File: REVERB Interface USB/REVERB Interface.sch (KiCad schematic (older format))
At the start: 73 parts, among them J1 RPiZeroW, J2 Iridium, J3 APRS, J4 Antenna, J6 USB_B_Micro, J7 USB, J8 USBPOGO, M1 MountingHole_Pad, M2 MountingHole_Pad, M3 MountingHole_Pad, M4 MountingHole_Pad, M5 PiMount, M6 PiMount, M7 PiMount, M8 PiMount, U1 IMU, U2 MAX3232, U3 CY7C65213-28PVXI, U4 TXB0104D, U5 DS3232M

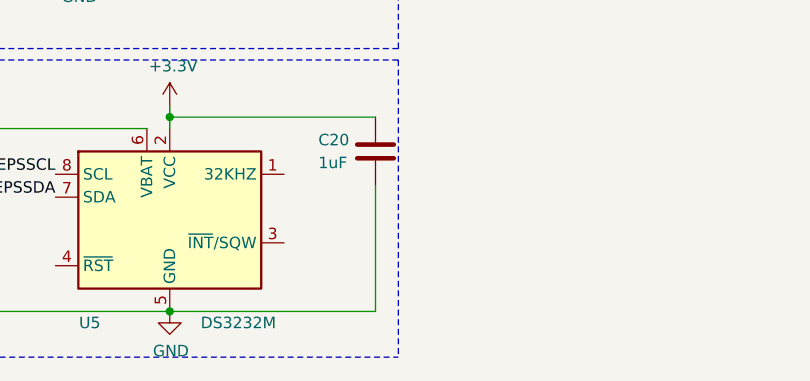
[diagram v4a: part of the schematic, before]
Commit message: add footprints, may need to use smaller battery
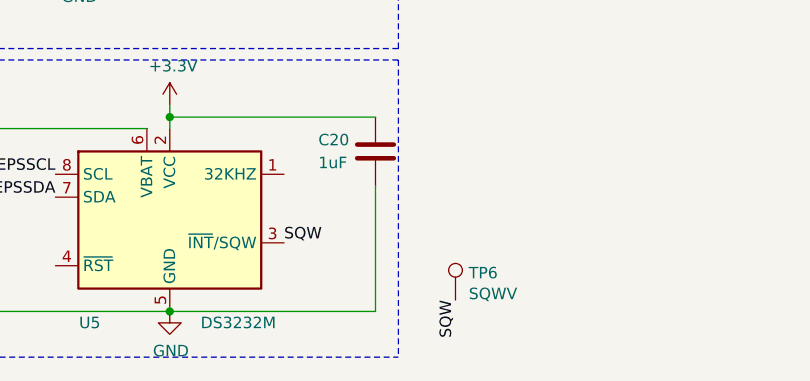
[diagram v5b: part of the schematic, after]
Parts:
- added TP6: SQWV, TestPoint:TestPoint_Pad_D2.0mm, symbol Connector:TestPoint
- BT1: footprint (none) -> REVERB Interface:CR2032-LINX-HLD-001-THM
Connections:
- net SQW: now reaches U5.3 (~INT~/SQW)
- net SQW: now also TP6.1
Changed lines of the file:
@@
 	6600 7000 4100 7000
 $Comp
-L Device:Battery_Cell BT1
-U 1 1 61948908
-P 4350 7700
-F 0 "BT1" H 4150 7850 50  0000 L CNN
-F 1 "CR-2032" H 4150 7650 50  0000 L CNN
-F 2 "" V 4350 7760 50  0001 C CNN
-F 3 "~" V 4350 7760 50  0001 C CNN
-	1    4350 7700
-	1    0    0    -1
-$EndComp
-$Comp
-L power:+3.3V #PWR?
+L power:+3.3V #PWR0135
 U 1 1 6194BC39
 P 5600 7200
-F 0 "#PWR?" H 5600 7050 50  0001 C CNN
+F 0 "#PWR0135" H 5600 7050 50  0001 C CNN
 F 1 "+3.3V" H 5615 7373 50  0000 C CNN
 F 2 "" H 5600 7200 50  0001 C CNN
@@
 	1    0    0    -1
 $EndComp
+Text Label 6100 7800 0    50   ~ 0
+SQW
+Text Label 6850 8050 3    50   ~ 0
+SQW
+$Comp
+L Connector:TestPoint TP6
+U 1 1 6194CAD9
+P 6850 8050
+F 0 "TP6" H 6908 8168 50  0000 L CNN
+F 1 "SQWV" H 6908 8077 50  0000 L CNN
+F 2 "TestPoint:TestPoint_Pad_D2.0mm" H 7050 8050 50  0001 C CNN
+F 3 "~" H 7050 8050 50  0001 C CNN
+	1    6850 8050
+	1    0    0    -1
+$EndComp
+$Comp
+L Device:Battery_Cell BT1
+U 1 1 61948908
+P 4350 7700
+F 0 "BT1" H 4150 7850 50  0000 L CNN
+F 1 "CR-2032" H 4150 7650 50  0000 L CNN
+F 2 "REVERB Interface:CR2032-LINX-HLD-001-THM" V 4350 7760 50  0001 C CNN
+F 3 "~" V 4350 7760 50  0001 C CNN
+	1    4350 7700
+	1    0    0    -1
+$EndComp

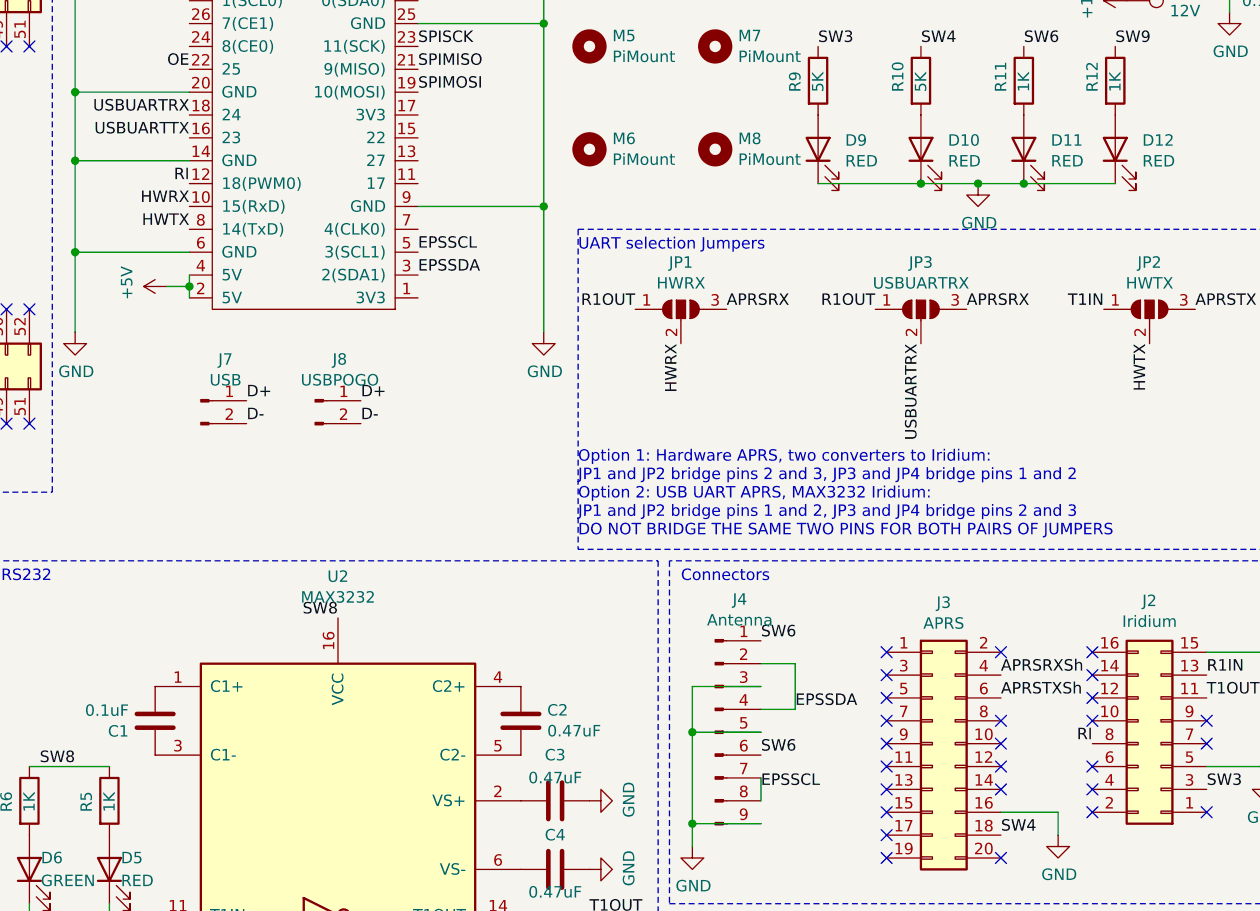
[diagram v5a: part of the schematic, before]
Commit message: Remove RI line
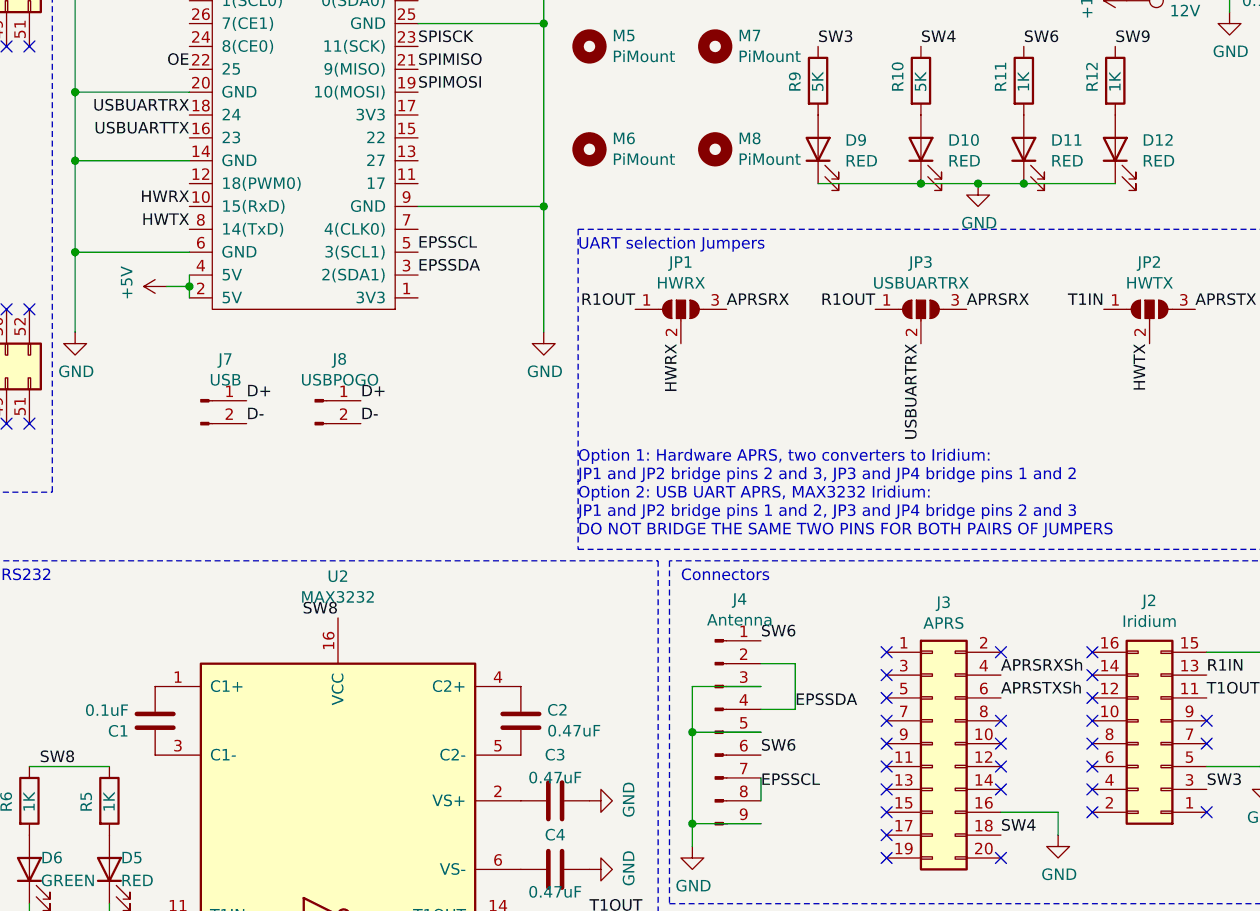
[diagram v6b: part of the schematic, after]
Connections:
- net RI: no longer names the net of J1.12 (18(PWM0))
- net RI: no longer J2.8 (Pin_8)
- no-connect marks 98 -> 99
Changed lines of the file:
@@
 Text Label 4550 1250 2    50   ~ 0
 IMURST
-Text Label 8500 4700 2    50   ~ 0
-RI
-Text Label 4550 2250 2    50   ~ 0
-RI
 Wire Wire Line
 	9250 4800 9250 4300
@@
 	1    0    0    -1
 $EndComp
+NoConn ~ 8500 4700
 $EndSCHEMATC

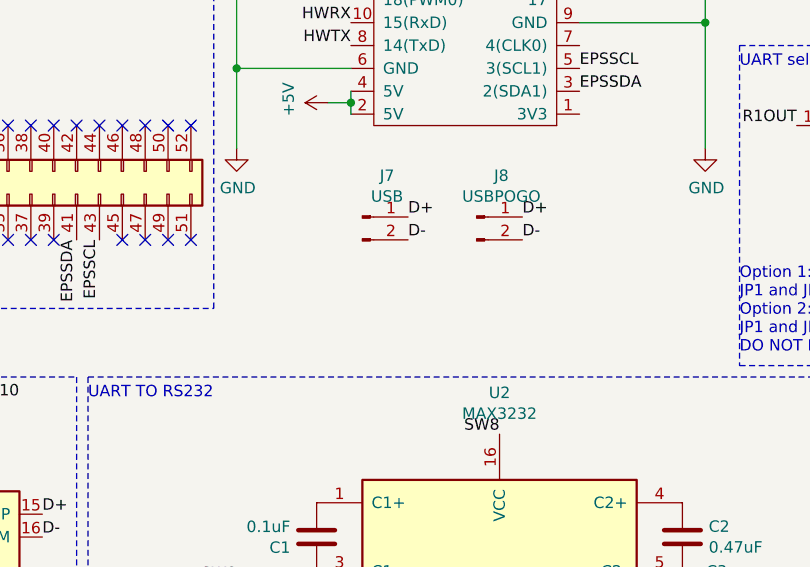
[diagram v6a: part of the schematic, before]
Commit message: add usb switch
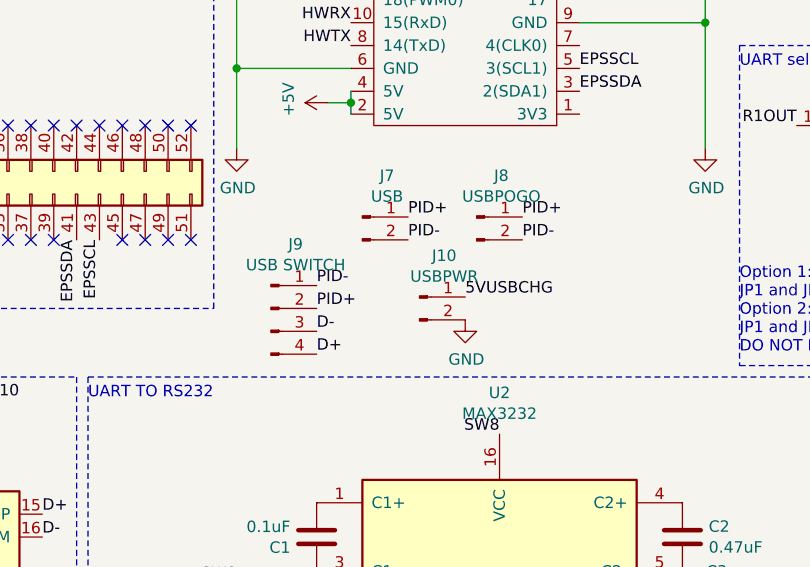
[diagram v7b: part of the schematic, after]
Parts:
- added J10: USBPWR, Connector_JST:JST_XH_B2B-XH-A_1x02_P2.50mm_Vertical, symbol Connector:Conn_01x02_Male
- added J9: USB SWITCH, Connector_JST:JST_XH_B4B-XH-A_1x04_P2.50mm_Vertical, symbol Connector:Conn_01x04_Male
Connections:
- net 5VUSBCHG: now also J10.1 (Pin_1)
- net D+: now also J9.4 (Pin_4); no longer J7.1 (Pin_1), J8.1 (Pin_1)
- net D-: now also J9.3 (Pin_3); no longer J7.2 (Pin_2), J8.2 (Pin_2)
- net GND: now also J10.2 (Pin_2)
- new net PID+: J7.1 (Pin_1), J8.1 (Pin_1), J9.2 (Pin_2)
- new net PID-: J7.2 (Pin_2), J8.2 (Pin_2), J9.1 (Pin_1)
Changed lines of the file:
@@
 $EndComp
 Text Label 4800 3200 0    50   ~ 0
-D+
+PID+
 Text Label 4800 3300 0    50   ~ 0
-D-
+PID-
 $Comp
 L Interface_UART:MAX3232 U2
@@
 $EndComp
 Text Label 5300 3200 0    50   ~ 0
-D+
+PID+
 Text Label 5300 3300 0    50   ~ 0
-D-
+PID-
 $Comp
 L Mechanical:MountingHole M5
@@
 $EndComp
 NoConn ~ 8500 4700
+$Comp
+L Connector:Conn_01x04_Male J9
+U 1 1 619777A4
+P 4200 3600
+F 0 "J9" H 4308 3881 50  0000 C CNN
+F 1 "USB SWITCH" H 4308 3790 50  0000 C CNN
+F 2 "Connector_JST:JST_XH_B4B-XH-A_1x04_P2.50mm_Vertical" H 4200 3600 50  0001 C CNN
+F 3 "~" H 4200 3600 50  0001 C CNN
+	1    4200 3600
+	1    0    0    -1
+$EndComp
+Text Label 4400 3600 0    50   ~ 0
+PID+
+Text Label 4400 3500 0    50   ~ 0
+PID-
+Text Label 4400 3800 0    50   ~ 0
+D+
+Text Label 4400 3700 0    50   ~ 0
+D-
+$Comp
+L Connector:Conn_01x02_Male J10
+U 1 1 61984053
+P 4850 3550
+F 0 "J10" H 4958 3731 50  0000 C CNN
+F 1 "USBPWR" H 4958 3640 50  0000 C CNN
+F 2 "Connector_JST:JST_XH_B2B-XH-A_1x02_P2.50mm_Vertical" H 4850 3550 50  0001 C CNN
+F 3 "~" H 4850 3550 50  0001 C CNN
+	1    4850 3550
+	1    0    0    -1
+$EndComp
+Text Label 5050 3550 0    50   ~ 0
+5VUSBCHG
+$Comp
+L power:GND #PWR0136
+U 1 1 6198E211
+P 5050 3650
+F 0 "#PWR0136" H 5050 3400 50  0001 C CNN
+F 1 "GND" H 5055 3477 50  0000 C CNN
+F 2 "" H 5050 3650 50  0001 C CNN
+F 3 "" H 5050 3650 50  0001 C CNN
+	1    5050 3650
+	1    0    0    -1
+$EndComp
 $EndSCHEMATC

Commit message: Move some parts around, remove UART LEDs, .step export, push v1.6
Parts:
- removed D1, D5: RED, LED_SMD:LED_0805_2012Metric_Pad1.15x1.40mm_HandSolder, symbol Device:LED
- removed D2, D6: GREEN, LED_SMD:LED_0805_2012Metric_Pad1.15x1.40mm_HandSolder, symbol Device:LED
- removed R1, R2, R5, R6: 1K, Resistor_SMD:R_0805_2012Metric_Pad1.20x1.40mm_HandSolder, symbol Device:R
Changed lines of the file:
@@
 Title "TJ REVERB Interface Board"
 Date "2021-10-03"
-Rev "1.5"
+Rev "1.6"
 Comp "TJ Nanosat Club"
 Comment1 "Redesign from previous Eagle designs"
@@
 $EndComp
 Wire Wire Line
-	2100 4700 1300 4700
-Wire Wire Line
-	2100 4800 1700 4800
-$Comp
-L Device:LED D1
-U 1 1 61680797
-P 1700 4450
-F 0 "D1" V 1739 4332 50  0000 R CNN
-F 1 "RED" V 1648 4332 50  0000 R CNN
-F 2 "LED_SMD:LED_0805_2012Metric_Pad1.15x1.40mm_HandSolder" H 1700 4450 50  0001 C CNN
-F 3 "~" H 1700 4450 50  0001 C CNN
-	1    1700 4450
-	0    -1   -1   0
-$EndComp
-$Comp
-L Device:LED D2
-U 1 1 61681979
-P 1300 4450
-F 0 "D2" V 1339 4332 50  0000 R CNN
-F 1 "GREEN" V 1248 4332 50  0000 R CNN
-F 2 "LED_SMD:LED_0805_2012Metric_Pad1.15x1.40mm_HandSolder" H 1300 4450 50  0001 C CNN
-F 3 "~" H 1300 4450 50  0001 C CNN
-	1    1300 4450
-	0    -1   -1   0
-$EndComp
-$Comp
-L Device:R R1
-U 1 1 61683EE4
-P 1700 4150
-F 0 "R1" V 1600 4100 50  0000 L CNN
-F 1 "1K" V 1700 4100 50  0000 L CNN
-F 2 "Resistor_SMD:R_0805_2012Metric_Pad1.20x1.40mm_HandSolder" V 1630 4150 50  0001 C CNN
-F 3 "~" H 1700 4150 50  0001 C CNN
-	1    1700 4150
-	1    0    0    -1
-$EndComp
-$Comp
-L Device:R R2
-U 1 1 6168462F
-P 1300 4150
-F 0 "R2" V 1200 4100 50  0000 L CNN
-F 1 "1K" V 1300 4100 50  0000 L CNN
-F 2 "Resistor_SMD:R_0805_2012Metric_Pad1.20x1.40mm_HandSolder" V 1230 4150 50  0001 C CNN
-F 3 "~" H 1300 4150 50  0001 C CNN
-	1    1300 4150
-	1    0    0    -1
-$EndComp
-Wire Wire Line
-	1300 4000 1700 4000
-Connection ~ 1700 4000
-Wire Wire Line
-	1700 4600 1700 4800
-Connection ~ 1700 4800
-Wire Wire Line
-	1700 4800 1200 4800
-Wire Wire Line
-	1300 4600 1300 4700
-Connection ~ 1300 4700
-Wire Wire Line
-	1300 4700 1200 4700
-Wire Wire Line
 	2600 4300 2600 4000
 $Comp
@@
 Wire Wire Line
 	3550 6100 4100 6100
-$Comp
-L Device:LED D5
-U 1 1 616CB109
-P 4200 5250
-F 0 "D5" V 4250 5200 50  0000 R CNN
-F 1 "RED" V 4150 5200 50  0000 R CNN
-F 2 "LED_SMD:LED_0805_2012Metric_Pad1.15x1.40mm_HandSolder" H 4200 5250 50  0001 C CNN
-F 3 "~" H 4200 5250 50  0001 C CNN
-	1    4200 5250
-	0    -1   -1   0
-$EndComp
-$Comp
-L Device:R R5
-U 1 1 616CB10F
-P 4200 4950
-F 0 "R5" V 4100 4900 50  0000 L CNN
-F 1 "1K" V 4200 4900 50  0000 L CNN
-F 2 "Resistor_SMD:R_0805_2012Metric_Pad1.20x1.40mm_HandSolder" V 4130 4950 50  0001 C CNN
-F 3 "~" H 4200 4950 50  0001 C CNN
-	1    4200 4950
-	1    0    0    -1
-$EndComp
-$Comp
-L Device:R R6
-U 1 1 616D0A78
-P 3850 4950
-F 0 "R6" V 3750 4900 50  0000 L CNN
-F 1 "1K" V 3850 4900 50  0000 L CNN
-F 2 "Resistor_SMD:R_0805_2012Metric_Pad1.20x1.40mm_HandSolder" V 3780 4950 50  0001 C CNN
-F 3 "~" H 3850 4950 50  0001 C CNN
-	1    3850 4950
-	1    0    0    -1
-$EndComp
-Text Label 4050 4800 2    50   ~ 0
-SW8
-$Comp
-L Device:LED D6
-U 1 1 616D0A72
-P 3850 5250
-F 0 "D6" V 3900 5200 50  0000 R CNN
-F 1 "GREEN" V 3800 5200 50  0000 R CNN
-F 2 "LED_SMD:LED_0805_2012Metric_Pad1.15x1.40mm_HandSolder" H 3850 5250 50  0001 C CNN
-F 3 "~" H 3850 5250 50  0001 C CNN
-	1    3850 5250
-	0    -1   -1   0
-$EndComp
-Wire Wire Line
-	4400 5450 4200 5450
-Wire Wire Line
-	3700 5850 3850 5850
-Wire Wire Line
-	3850 4800 4200 4800
 Wire Wire Line
 	6000 5450 6300 5450
 Wire Wire Line
 	6000 5850 6300 5850
-Wire Wire Line
-	4200 5400 4200 5450
-Connection ~ 4200 5450
-Wire Wire Line
-	4200 5450 3700 5450
-Wire Wire Line
-	3850 5400 3850 5850
-Connection ~ 3850 5850
-Wire Wire Line
-	3850 5850 4400 5850
 Text Notes 550  4900 0    50   ~ 0
 Micro B for programming
@@
 $EndComp
 Wire Wire Line
-	1700 4000 2600 4000
-Wire Wire Line
 	2700 4300 2700 4000
 Wire Wire Line
@@
 Wire Wire Line
 	2600 4000 2700 4000
-Connection ~ 2600 4000
 Connection ~ 2700 4000
 Text Label 900  6000 1    50   ~ 0
@@
 	1    0    0    -1
 $EndComp
+Wire Wire Line
+	1200 4800 2100 4800
+Wire Wire Line
+	1200 4700 2100 4700
+Wire Wire Line
+	3700 5450 4400 5450
+Wire Wire Line
+	3700 5850 4400 5850
 $EndSCHEMATC
